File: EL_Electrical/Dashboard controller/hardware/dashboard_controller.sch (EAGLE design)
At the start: 51 parts, among them IC1 MCP2562-E_SN, IC2 MCP2515-I_SO, J1 22-05-7098-09, Q1 BSS138, Q4 BSS138, Q5 BSS138, Q6 BSS138

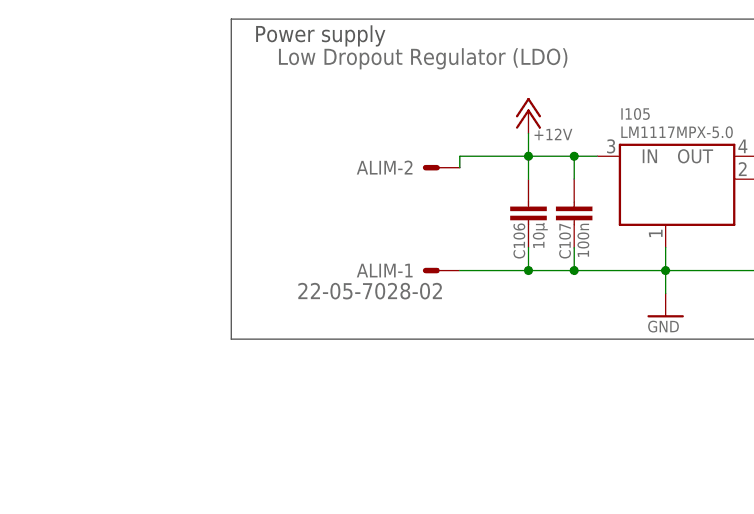
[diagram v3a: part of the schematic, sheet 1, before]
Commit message: Add capacitors (470uF: about 18,20mm x 10,8mm; Footprint utilisé 25mm x 10mm)
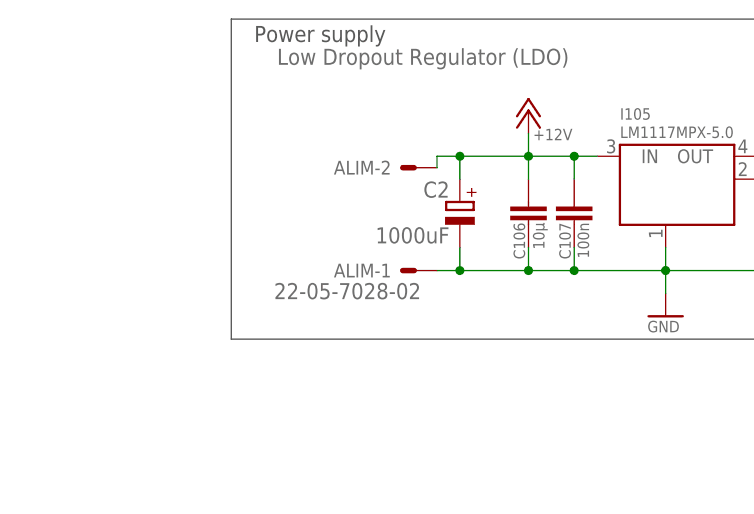
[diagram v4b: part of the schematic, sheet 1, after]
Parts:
- added C2: 1000uF, rcl:CPOL-EUE25-10AXIAL
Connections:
- net +12V: now also C2.+
- net GND: now also C2.-
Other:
- moved on the sheet: ALIM-1, ALIM-2
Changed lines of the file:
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@@
 <part name="P+2" library="supply1" library_urn="urn:adsk.eagle:library:371" deviceset="+5V" device=""/>
 <part name="TEST_PINS" library="test_pin_DTA" deviceset="PINHD-1X8" device="" package3d_urn="urn:adsk.eagle:package:22409/2"/>
+<part name="C2" library="rcl" library_urn="urn:adsk.eagle:library:334" deviceset="CPOL-EU" device="E25-10AXIAL" package3d_urn="urn:adsk.eagle:package:23352/1" value="1000uF"/>
 </parts>
 <sheets>
@@
 <attribute name="VALUE" x="190.5" y="200.66" size="1.778" layer="96" rot="R180"/>
 </instance>
-<instance part="ALIM" gate="-1" x="50.8" y="195.58" smashed="yes" rot="R180">
-<attribute name="NAME" x="48.26" y="196.342" size="1.524" layer="95" rot="R180"/>
-<attribute name="VALUE" x="51.562" y="194.183" size="1.778" layer="96" rot="R180"/>
-</instance>
-<instance part="ALIM" gate="-2" x="50.8" y="207.01" smashed="yes" rot="R180">
-<attribute name="NAME" x="48.26" y="207.772" size="1.524" layer="95" rot="R180"/>
+<instance part="ALIM" gate="-1" x="48.26" y="195.58" smashed="yes" rot="R180">
+<attribute name="NAME" x="45.72" y="196.342" size="1.524" layer="95" rot="R180"/>
+<attribute name="VALUE" x="49.022" y="194.183" size="1.778" layer="96" rot="R180"/>
+</instance>
+<instance part="ALIM" gate="-2" x="48.26" y="207.01" smashed="yes" rot="R180">
+<attribute name="NAME" x="45.72" y="207.772" size="1.524" layer="95" rot="R180"/>
 </instance>
 <instance part="GND" gate="G$1" x="251.46" y="17.78" smashed="yes">
@@
 <attribute name="NAME" x="283.21" y="76.835" size="1.778" layer="95"/>
 <attribute name="VALUE" x="283.21" y="50.8" size="1.778" layer="96"/>
+</instance>
+<instance part="C2" gate="G$1" x="53.34" y="203.2" smashed="yes" rot="MR0">
+<attribute name="NAME" x="52.197" y="203.6826" size="1.778" layer="95" rot="MR0"/>
+<attribute name="VALUE" x="52.197" y="198.6026" size="1.778" layer="96" rot="MR0"/>
 </instance>
 </instances>
@@
 <junction x="60.96" y="208.28"/>
 <pinref part="P+11" gate="1" pin="+12V"/>
+<wire x1="53.34" y1="208.28" x2="60.96" y2="208.28" width="0.1524" layer="91"/>
+<pinref part="C2" gate="G$1" pin="+"/>
+<wire x1="53.34" y1="208.28" x2="53.34" y2="205.74" width="0.1524" layer="91"/>
 <pinref part="ALIM" gate="-2" pin="S"/>
-<wire x1="53.34" y1="207.01" x2="53.34" y2="208.28" width="0.1524" layer="91"/>
-<wire x1="53.34" y1="208.28" x2="60.96" y2="208.28" width="0.1524" layer="91"/>
+<junction x="53.34" y="208.28"/>
+<wire x1="53.34" y1="208.28" x2="50.8" y2="208.28" width="0.1524" layer="91"/>
+<wire x1="50.8" y1="208.28" x2="50.8" y2="207.01" width="0.1524" layer="91"/>
 </segment>
 </net>
@@
 <wire x1="60.96" y1="195.58" x2="53.34" y2="195.58" width="0.1524" layer="91"/>
 <junction x="60.96" y="195.58"/>
-</segment>
-<segment>
+<pinref part="C2" gate="G$1" pin="-"/>
+<wire x1="53.34" y1="195.58" x2="50.8" y2="195.58" width="0.1524" layer="91"/>
+<wire x1="53.34" y1="198.12" x2="53.34" y2="195.58" width="0.1524" layer="91"/>
+<junction x="53.34" y="195.58"/>
+</segment>
+<segment>

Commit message: Delete useless resistors (Dashboard_controller)
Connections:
- removed net GEAR_POT: U$1.A14/DAC
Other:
- note removed: "GEAR_POT_ANALOG"
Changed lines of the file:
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@@
 <text x="181.61" y="161.29" size="1.27" layer="97">G</text>
 <text x="186.69" y="158.75" size="1.27" layer="97">D</text>
-<text x="109.22" y="93.98" size="1.778" layer="94">GEAR_POT_ANALOG</text>
 <wire x1="228.6" y1="223.52" x2="152.4" y2="223.52" width="0.1524" layer="97"/>
 <wire x1="152.4" y1="223.52" x2="152.4" y2="27.94" width="0.1524" layer="97"/>
@@
 <wire x1="203.2" y1="96.52" x2="203.2" y2="105.41" width="0.1524" layer="91"/>
 <pinref part="GND3" gate="1" pin="GND"/>
+<junction x="203.2" y="96.52"/>
 </segment>
 <segment>
@@
 <wire x1="203.2" y1="53.34" x2="203.2" y2="62.23" width="0.1524" layer="91"/>
 <pinref part="GND4" gate="1" pin="GND"/>
+<junction x="203.2" y="53.34"/>
 </segment>
 <segment>
@@
 </segment>
 </net>
-<net name="GEAR_POT" class="0">
-<segment>
-<pinref part="U$1" gate="G$1" pin="A14/DAC"/>
-<wire x1="105.41" y1="97.79" x2="109.22" y2="97.79" width="0.1524" layer="91"/>
-<wire x1="109.22" y1="97.79" x2="109.22" y2="99.06" width="0.1524" layer="91"/>
-<wire x1="109.22" y1="99.06" x2="111.76" y2="99.06" width="0.1524" layer="91"/>
-<label x="111.76" y="99.06" size="1.778" layer="95" xref="yes"/>
-</segment>
-</net>

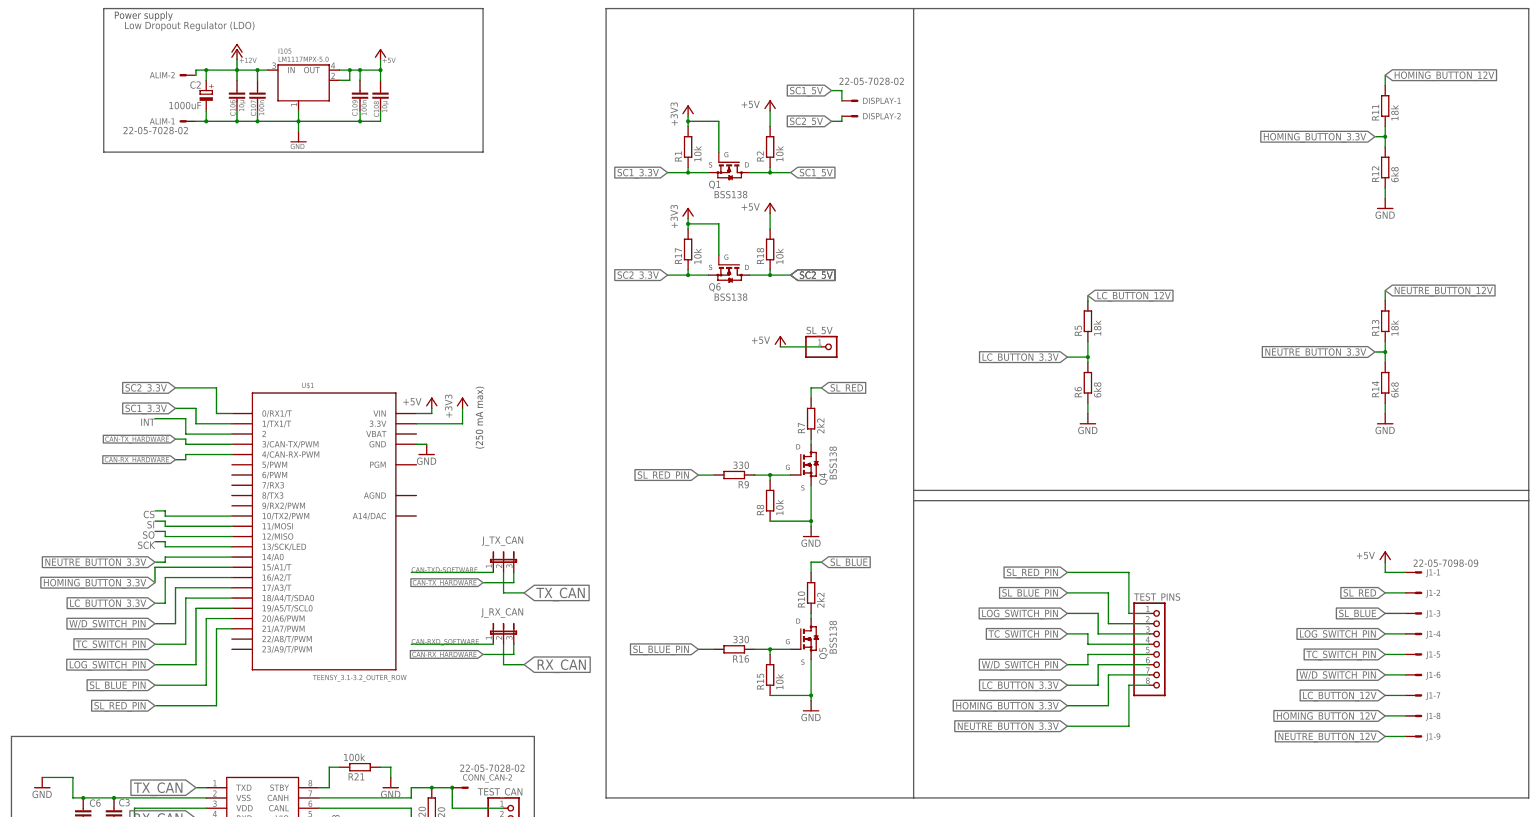
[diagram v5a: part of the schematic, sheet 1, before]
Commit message: Delete useless resistors (Dashboard_controller)
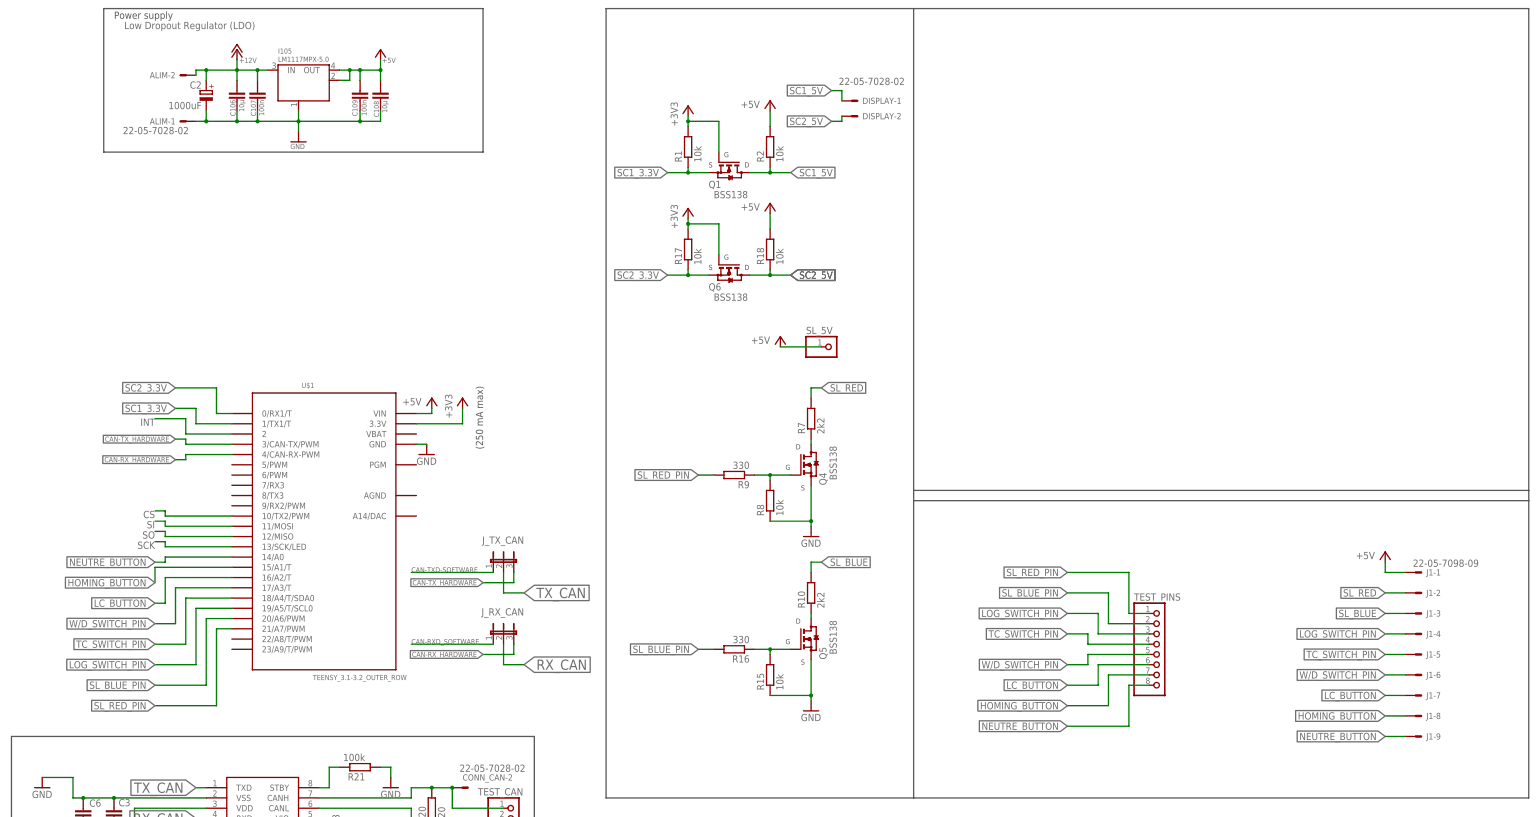
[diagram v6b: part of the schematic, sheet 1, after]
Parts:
- removed R11, R13, R5: 18k, rcl:R-EU_R0805
- removed R12, R14, R6: 6k8, rcl:R-EU_R0805
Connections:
- removed net HOMING_BUTTON_12V: J1-8.S, R11.2
- removed net HOMING_BUTTON_3.3V: R11.1, R12.2, TEST_PINS.7, U$1.15/A1/T
- removed net LC_BUTTON_12V: J1-7.S, R5.2
- removed net LC_BUTTON_3.3V: R5.1, R6.2, TEST_PINS.6, U$1.16/A2/T
- removed net NEUTRE_BUTTON_12V: J1-9.S, R13.2
- removed net NEUTRE_BUTTON_3.3V: R13.1, R14.2, TEST_PINS.8, U$1.14/A0
- new net HOMING_BUTTON: J1-8.S, TEST_PINS.7, U$1.15/A1/T
- new net LC_BUTTON: J1-7.S, TEST_PINS.6, U$1.16/A2/T
- new net NEUTRE_BUTTON: J1-9.S, TEST_PINS.8, U$1.14/A0
- net GND: no longer R12.1, R14.1, R6.1

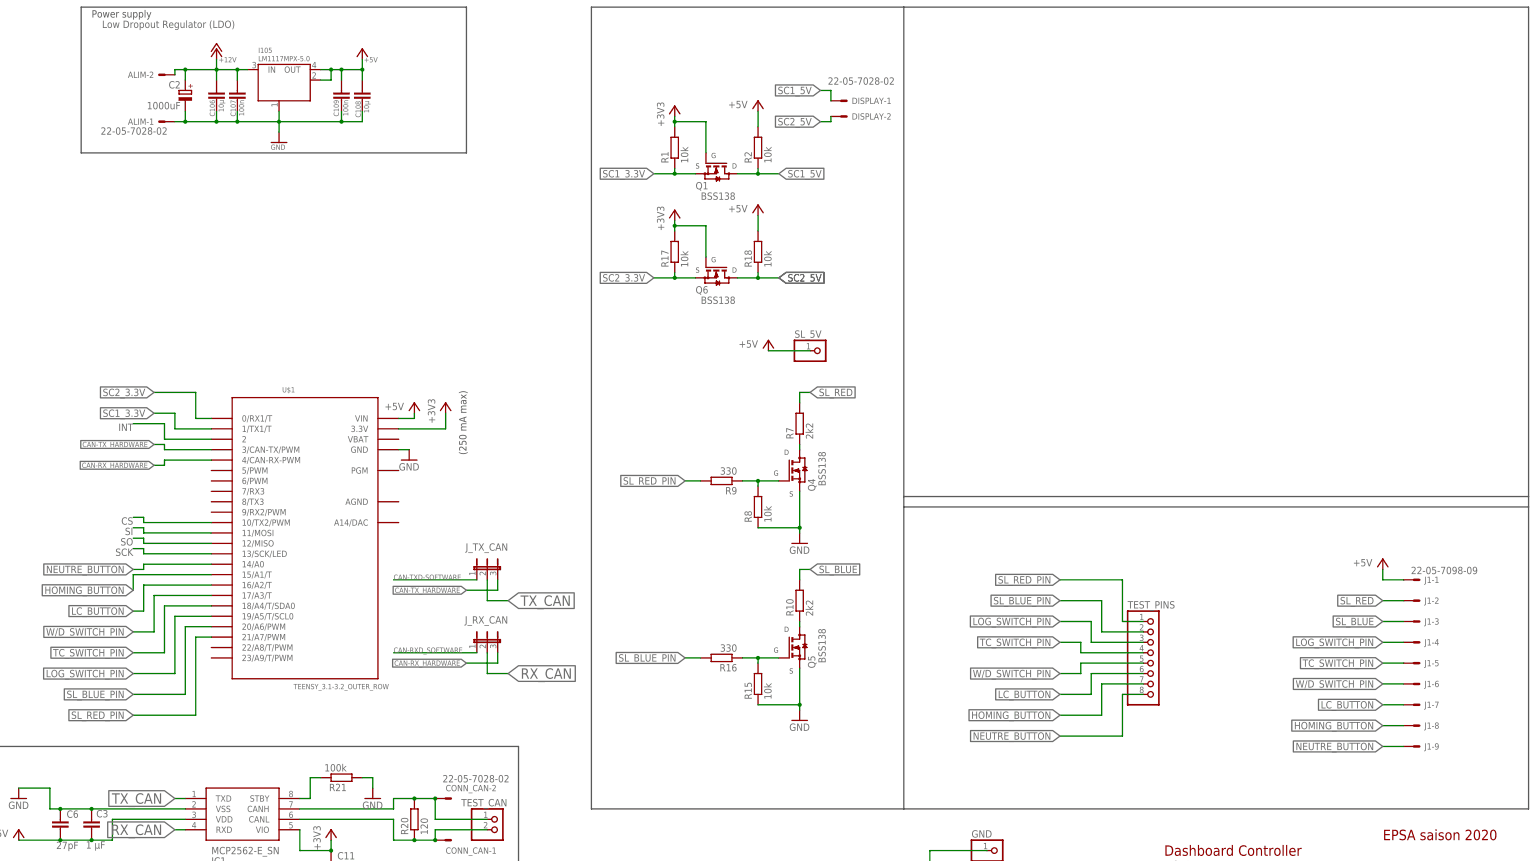
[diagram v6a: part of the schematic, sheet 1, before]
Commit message: Change connector footprint, LDO regulator (DC linear voltage regulator) position and reduce the size
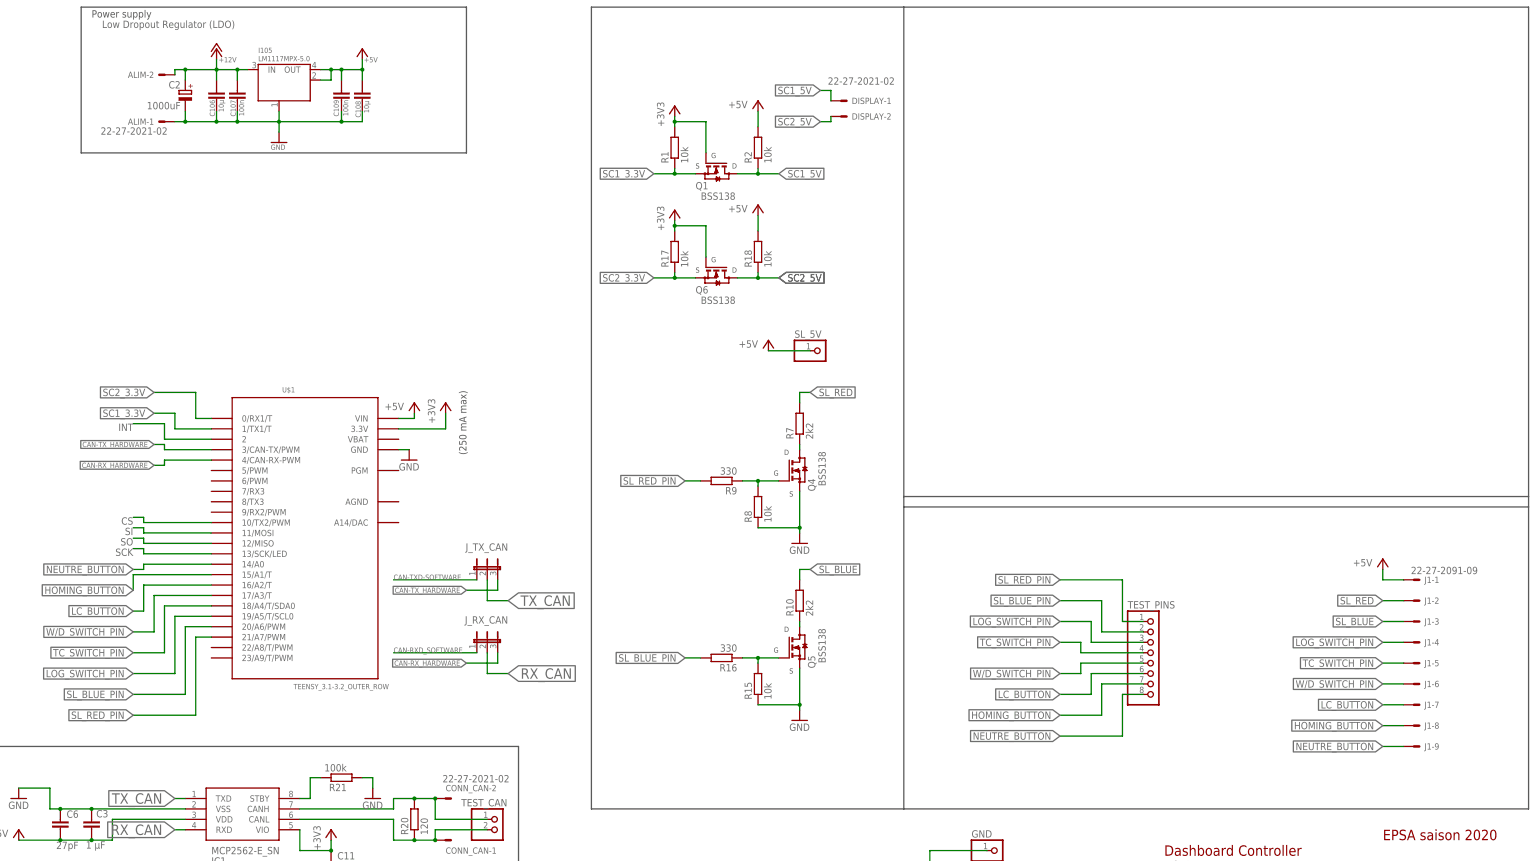
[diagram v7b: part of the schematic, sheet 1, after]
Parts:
- ALIM, DISPLAY: value 22-05-7028-02 -> 22-27-2021-02; device EP_molex_6410_7395:22-05-7028-02 -> con-molex:22-27-2021-02
- CONN_CAN: value 22-05-7028-02 -> 22-27-2021-02; device con-molex:22-05-7028-02 -> con-molex:22-27-2021-02
- J1: value 22-05-7098-09 -> 22-27-2091-09; device con-molex:22-05-7098-09 -> con-molex:22-27-2091-09
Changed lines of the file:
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@@
 <part name="FRAME2" library="frames" library_urn="urn:adsk.eagle:library:229" deviceset="A4L-LOC" device=""/>
 <part name="+3V7" library="supply1" library_urn="urn:adsk.eagle:library:371" deviceset="+3V3" device=""/>
-<part name="CONN_CAN" library="con-molex" library_urn="urn:adsk.eagle:library:165" deviceset="22-?-02" device="05-7028" package3d_urn="urn:adsk.eagle:package:8078644/1"/>
+<part name="CONN_CAN" library="con-molex" library_urn="urn:adsk.eagle:library:165" deviceset="22-?-02" device="27-2021" package3d_urn="urn:adsk.eagle:package:8078645/1" value="22-27-2021-02"/>
 <part name="R20" library="rcl" library_urn="urn:adsk.eagle:library:334" deviceset="R-EU_" device="R0805" package3d_urn="urn:adsk.eagle:package:23553/2" value="120 "/>
 <part name="GND14" library="supply1" deviceset="GND" device=""/>
@@
 <part name="+3V6" library="supply1" library_urn="urn:adsk.eagle:library:371" deviceset="+3V3" device=""/>
 <part name="P+13" library="supply1" library_urn="urn:adsk.eagle:library:371" deviceset="+5V" device=""/>
-<part name="ALIM" library="EP_molex_6410_7395" deviceset="22-?-02" device="05-7028"/>
+<part name="ALIM" library="con-molex" library_urn="urn:adsk.eagle:library:165" deviceset="22-?-02" device="27-2021" package3d_urn="urn:adsk.eagle:package:8078645/1"/>
 <part name="R23" library="rcl" library_urn="urn:adsk.eagle:library:334" deviceset="R-EU_" device="R0805" package3d_urn="urn:adsk.eagle:package:23553/2" value="1k"/>
 <part name="+3V1" library="supply1" library_urn="urn:adsk.eagle:library:371" deviceset="+3V3" device=""/>
@@
 <part name="+3V10" library="supply1" library_urn="urn:adsk.eagle:library:371" deviceset="+3V3" device=""/>
 <part name="P+1" library="supply1" library_urn="urn:adsk.eagle:library:371" deviceset="+5V" device=""/>
-<part name="DISPLAY" library="EP_molex_6410_7395" deviceset="22-?-02" device="05-7028"/>
-<part name="J1" library="con-molex" library_urn="urn:adsk.eagle:library:165" deviceset="22-?-09" device="05-7098" package3d_urn="urn:adsk.eagle:package:8078658/1"/>
+<part name="DISPLAY" library="con-molex" library_urn="urn:adsk.eagle:library:165" deviceset="22-?-02" device="27-2021" package3d_urn="urn:adsk.eagle:package:8078645/1"/>
+<part name="J1" library="con-molex" library_urn="urn:adsk.eagle:library:165" deviceset="22-?-09" device="27-2091" package3d_urn="urn:adsk.eagle:package:8078659/1" value="22-27-2091-09"/>
 <part name="R7" library="rcl" library_urn="urn:adsk.eagle:library:334" deviceset="R-EU_" device="R0805" package3d_urn="urn:adsk.eagle:package:23553/2" value="2k2"/>
 <part name="P+4" library="supply1" library_urn="urn:adsk.eagle:library:371" deviceset="+5V" device=""/>
